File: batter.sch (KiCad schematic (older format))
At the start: 10 parts, among them P1 CONN_2, U2 MCP73831-SOT-23-5, U3 NCP4681-SC-70

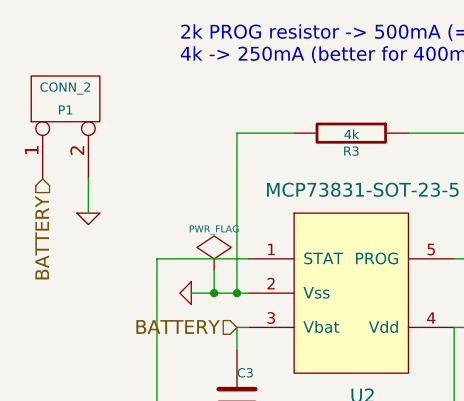
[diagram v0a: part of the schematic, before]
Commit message: Start implementing new version: move USB port and altimeter module, new buzzer and volume control
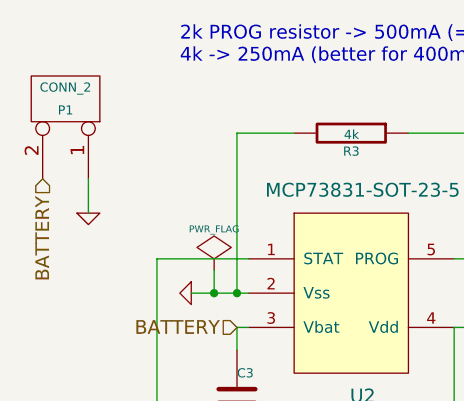
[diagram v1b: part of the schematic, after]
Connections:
- net BATTERY: now also P1.2 (PM); no longer P1.1 (P1)
- net GND: now also P1.1 (P1); no longer P1.2 (PM)
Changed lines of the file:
@@
 F 3 "" H 2550 1350 60  0000 C CNN
 	1    2550 1350
-	0    -1   -1   0
+	0    1    -1   0
 $EndComp
 Text HLabel 2450 1700 3    60   Input ~ 0

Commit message: Before starting laying out tracks
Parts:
- added U15: SPDT-SWITCH, buq2:CUS-12TB-SWITCH, symbol SPDT-SWITCH
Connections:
- net BATTERY: now also U15.2; no longer P1.2 (PM)
- new net BATTERY-DIRECT: P1.2 (PM), U15.1
- no-connect marks 1 -> 2
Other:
- moved on the sheet: P1
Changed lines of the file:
@@
 $Descr A4 11693 8268
 encoding utf-8
-Sheet 3 10
+Sheet 3 11
 Title ""
 Date ""
@@
 	3300 2900 3300 2850
 Wire Wire Line
-	3350 2350 3300 2350
+	3250 2350 3350 2350
 Wire Wire Line
 	3300 2350 3300 2450
@@
 Wire Wire Line
 	5600 2900 5750 2900
-Text HLabel 3300 2350 0    60   Input ~ 0
+Text HLabel 2350 2650 2    60   Input ~ 0
 BATTERY
 $Comp
@@
 L CONN_2 P1
 U 1 1 5461388F
-P 2550 1350
-F 0 "P1" V 2500 1350 40  0000 C CNN
-F 1 "CONN_2" V 2600 1350 40  0000 C CNN
-F 2 "buq2:PIN_HEADER_2" H 2550 1350 60  0001 C CNN
-F 3 "" H 2550 1350 60  0000 C CNN
-	1    2550 1350
+P 2300 800
+F 0 "P1" V 2250 800 40  0000 C CNN
+F 1 "CONN_2" V 2350 800 40  0000 C CNN
+F 2 "buq2:PIN_HEADER_2" H 2300 800 60  0001 C CNN
+F 3 "" H 2300 800 60  0000 C CNN
+	1    2300 800
 	0    1    -1   0
 $EndComp
-Text HLabel 2450 1700 3    60   Input ~ 0
+Text HLabel 3250 2350 0    60   Input ~ 0
 BATTERY
 $Comp
 L GND #PWR010
 U 1 1 546139D5
-P 2650 1850
-F 0 "#PWR010" H 2650 1850 30  0001 C CNN
-F 1 "GND" H 2650 1780 30  0001 C CNN
-F 2 "" H 2650 1850 60  0000 C CNN
-F 3 "" H 2650 1850 60  0000 C CNN
-	1    2650 1850
+P 2400 1300
+F 0 "#PWR010" H 2400 1300 30  0001 C CNN
+F 1 "GND" H 2400 1230 30  0001 C CNN
+F 2 "" H 2400 1300 60  0000 C CNN
+F 3 "" H 2400 1300 60  0000 C CNN
+	1    2400 1300
 	1    0    0    -1
 $EndComp
@@
 Connection ~ 6950 2600
 Wire Wire Line
-	2650 1700 2650 1850
+	2400 1150 2400 1300
 $Comp
 L PWR_FLAG #FLG012
@@
 Text HLabel 6750 2350 1    60   Input ~ 0
 BATTERY
+Text Label 2200 1150 3    60   ~ 0
+BATTERY-DIRECT
+Text Label 1450 2500 2    60   ~ 0
+BATTERY-DIRECT
+NoConn ~ 1550 2800
+Wire Wire Line
+	2350 2650 2300 2650
+Wire Wire Line
+	1450 2500 1550 2500
+Connection ~ 3300 2350
+$Comp
+L SPDT-SWITCH U15
+U 1 1 5530055B
+P 1900 2650
+F 0 "U15" H 1900 2350 60  0000 C CNN
+F 1 "SPDT-SWITCH" H 1900 2900 60  0000 C CNN
+F 2 "buq2:CUS-12TB-SWITCH" H 1850 2650 60  0001 C CNN
+F 3 "" H 1850 2650 60  0000 C CNN
+	1    1900 2650
+	1    0    0    -1
+$EndComp
 $EndSCHEMATC

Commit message: Some changes?
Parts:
- added R10, R9: 500k, buq2:SM0603, symbol R
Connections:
- net BATTERY: now also R9.1
- net GND: now also R10.2
- new net BATTERY_SENSE: R10.1, R9.2
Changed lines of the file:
@@
 $Descr A4 11693 8268
 encoding utf-8
-Sheet 3 11
+Sheet 3 10
 Title ""
 Date ""
@@
 $EndComp
 $Comp
-L GND #PWR04
+L GND #PWR6
 U 1 1 54461EBB
 P 3100 2200
-F 0 "#PWR04" H 3100 2200 30  0001 C CNN
+F 0 "#PWR6" H 3100 2200 30  0001 C CNN
 F 1 "GND" H 3100 2130 30  0001 C CNN
 F 2 "" H 3100 2200 60  0000 C CNN
@@
 $EndComp
 $Comp
-L GND #PWR05
+L GND #PWR18
 U 1 1 54461ED8
 P 4400 2900
-F 0 "#PWR05" H 4400 2900 30  0001 C CNN
+F 0 "#PWR18" H 4400 2900 30  0001 C CNN
 F 1 "GND" H 4400 2830 30  0001 C CNN
 F 2 "" H 4400 2900 60  0000 C CNN
@@
 $EndComp
 $Comp
-L GND #PWR06
+L GND #PWR7
 U 1 1 54461EDE
 P 3300 2900
-F 0 "#PWR06" H 3300 2900 30  0001 C CNN
+F 0 "#PWR7" H 3300 2900 30  0001 C CNN
 F 1 "GND" H 3300 2830 30  0001 C CNN
 F 2 "" H 3300 2900 60  0000 C CNN
@@
 NoConn ~ 5750 2750
 $Comp
-L GND #PWR07
+L GND #PWR29
 U 1 1 5446543B
 P 5600 2900
-F 0 "#PWR07" H 5600 2900 30  0001 C CNN
+F 0 "#PWR29" H 5600 2900 30  0001 C CNN
 F 1 "GND" H 5600 2830 30  0001 C CNN
 F 2 "" H 5600 2900 60  0000 C CNN
@@
 	7200 2600 7200 2500
 $Comp
-L GND #PWR08
+L GND #PWR30
 U 1 1 54613131
 P 7200 2100
-F 0 "#PWR08" H 7200 2100 30  0001 C CNN
+F 0 "#PWR30" H 7200 2100 30  0001 C CNN
 F 1 "GND" H 7200 2030 30  0001 C CNN
 F 2 "" H 7200 2100 60  0000 C CNN
@@
 	7200 2900 7200 3000
 $Comp
-L GND #PWR09
+L GND #PWR31
 U 1 1 5461320E
 P 7200 3400
-F 0 "#PWR09" H 7200 3400 30  0001 C CNN
+F 0 "#PWR31" H 7200 3400 30  0001 C CNN
 F 1 "GND" H 7200 3330 30  0001 C CNN
 F 2 "" H 7200 3400 60  0000 C CNN
@@
 BATTERY
 $Comp
-L GND #PWR010
+L GND #PWR2
 U 1 1 546139D5
 P 2400 1300
-F 0 "#PWR010" H 2400 1300 30  0001 C CNN
+F 0 "#PWR2" H 2400 1300 30  0001 C CNN
 F 1 "GND" H 2400 1230 30  0001 C CNN
 F 2 "" H 2400 1300 60  0000 C CNN
@@
 $EndComp
 $Comp
-L PWR_FLAG #FLG011
+L PWR_FLAG #FLG2
 U 1 1 54649A02
 P 6950 2550
-F 0 "#FLG011" H 6950 2645 30  0001 C CNN
+F 0 "#FLG2" H 6950 2645 30  0001 C CNN
 F 1 "PWR_FLAG" H 6950 2730 30  0000 C CNN
 F 2 "" H 6950 2550 60  0000 C CNN
@@
 	2400 1150 2400 1300
 $Comp
-L PWR_FLAG #FLG012
+L PWR_FLAG #FLG1
 U 1 1 5463E2BC
 P 3200 2100
-F 0 "#FLG012" H 3200 2195 30  0001 C CNN
+F 0 "#FLG1" H 3200 2195 30  0001 C CNN
 F 1 "PWR_FLAG" H 3200 2280 30  0000 C CNN
 F 2 "" H 3200 2100 60  0000 C CNN
@@
 	1    0    0    -1
 $EndComp
+Text HLabel 3050 4250 1    60   Input ~ 0
+BATTERY
+$Comp
+L R R9
+U 1 1 55EC56F8
+P 3050 4500
+F 0 "R9" V 3130 4500 40  0000 C CNN
+F 1 "500k" V 3057 4501 40  0000 C CNN
+F 2 "buq2:SM0603" V 2980 4500 30  0001 C CNN
+F 3 "" H 3050 4500 30  0000 C CNN
+	1    3050 4500
+	1    0    0    -1
+$EndComp
+$Comp
+L R R10
+U 1 1 55EC572D
+P 3050 5000
+F 0 "R10" V 3130 5000 40  0000 C CNN
+F 1 "500k" V 3057 5001 40  0000 C CNN
+F 2 "buq2:SM0603" V 2980 5000 30  0001 C CNN
+F 3 "" H 3050 5000 30  0000 C CNN
+	1    3050 5000
+	1    0    0    -1
+$EndComp
+$Comp
+L GND #PWR5
+U 1 1 55EC5789
+P 3050 5250
+F 0 "#PWR5" H 3050 5250 30  0001 C CNN
+F 1 "GND" H 3050 5180 30  0001 C CNN
+F 2 "" H 3050 5250 60  0000 C CNN
+F 3 "" H 3050 5250 60  0000 C CNN
+	1    3050 5250
+	1    0    0    -1
+$EndComp
+Text HLabel 2750 4750 0    60   Input ~ 0
+BATTERY_SENSE
+Wire Wire Line
+	2750 4750 3050 4750
 $EndSCHEMATC
